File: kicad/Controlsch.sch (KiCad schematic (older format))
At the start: 8 parts

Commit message: Updates and new features
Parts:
- added C303: 10μF, symbol Device:C
- added D301: LED_RAGB, symbol Device:LED_RAGB
- added Q301, Q302, Q303: Q_NMOS_DGS, symbol Device:Q_NMOS_DGS
- added R302: 10kΩ, Resistor_SMD:R_0805_2012Metric, symbol Device:R
- added R303: 1kΩ, Resistor_SMD:R_0805_2012Metric, symbol Device:R
- added R304, R305, R306: 470Ω, Resistor_SMD:R_0805_2012Metric, symbol Device:R
- added SW301: SW_SPST, symbol Switch:SW_SPST
- added U303: 7414, symbol 74xx_IEEE:7414
- C301, C302: renamed from C?; footprint (none) -> Capacitor_SMD:C_0805_2012Metric
- R301: renamed from R?; footprint (none) -> Resistor_SMD:R_0805_2012Metric
- gave numbers to parts that had none: 5
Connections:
- net labels added: LED_BLU, LED_GRN, LED_RED, RxD_DIN, SW_01, TxD_DOUT
- wire segments 31 -> 82
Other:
- note added: "Board Temperature\n- There is an internal temperature \n sensor in the MCU"

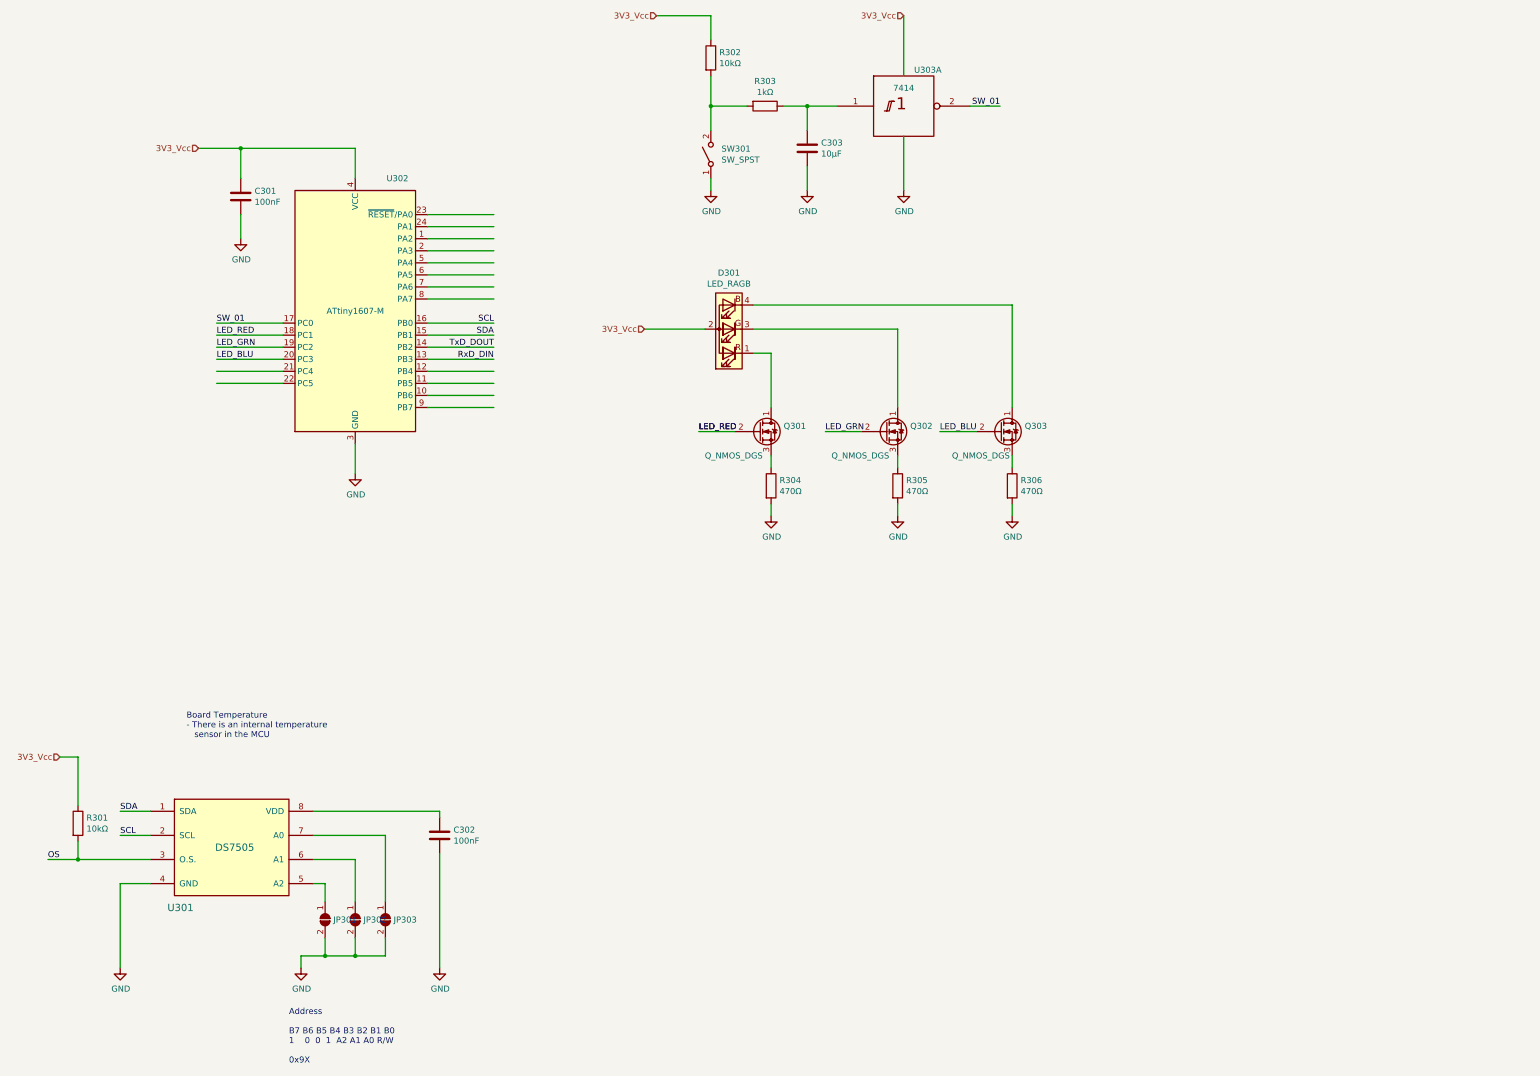
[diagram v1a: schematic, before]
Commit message: Updated the addresssing of the LCD
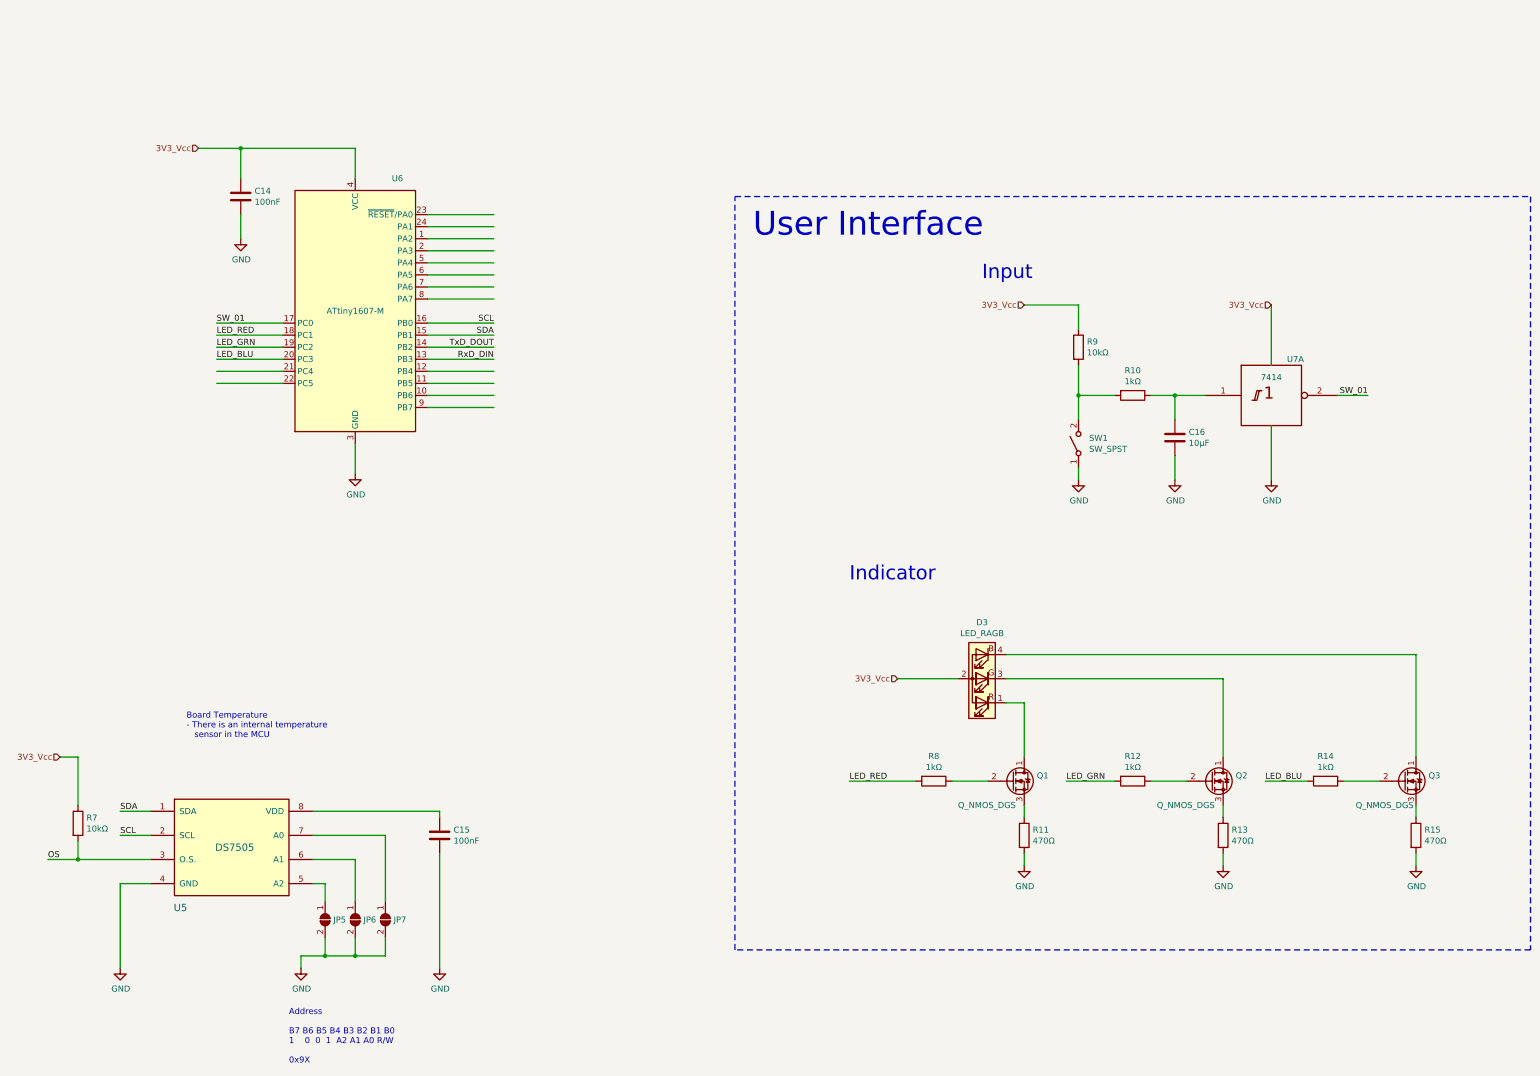
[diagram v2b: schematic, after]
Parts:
- added R12, R14, R8: 1kΩ, Resistor_SMD:R_0805_2012Metric, symbol Device:R
- renumbered C301 to C14, C302 to C15, C303 to C16, D301 to D3, JP301 to JP5, JP302 to JP6, JP303 to JP7, Q301 to Q1, Q302 to Q2, Q303 to Q3, R303 to R10, R304 to R11, R305 to R13, R306 to R15, R301 to R7, R302 to R9, SW301 to SW1, U301 to U5, U302 to U6, U303 to U7
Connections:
- wire segments 82 -> 85
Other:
- note added: "Indicator"
- note added: "Input"
- note added: "User Interface"
- moved on the sheet: C16, D3, Q1, Q2, Q3, R10, R11, R13, R15, R9, SW1, U7A

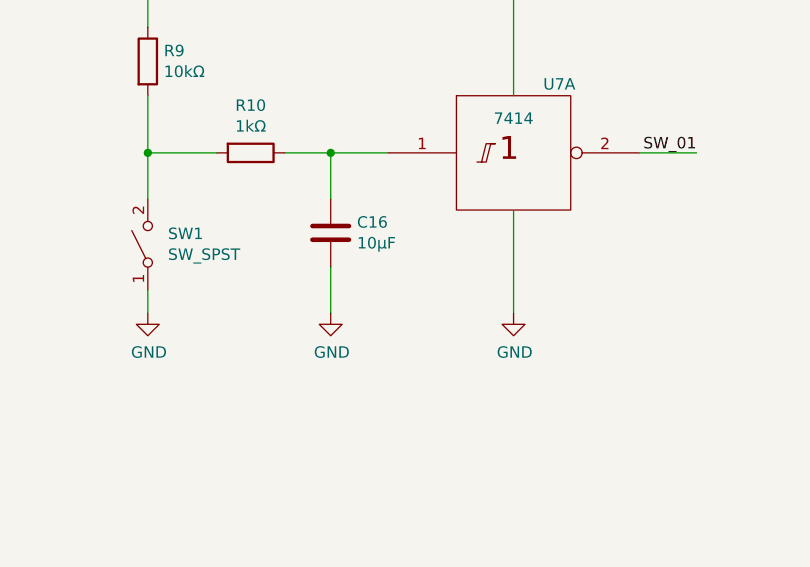
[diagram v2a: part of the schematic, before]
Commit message: Added a note about the capacitor for the de-bounce circuit
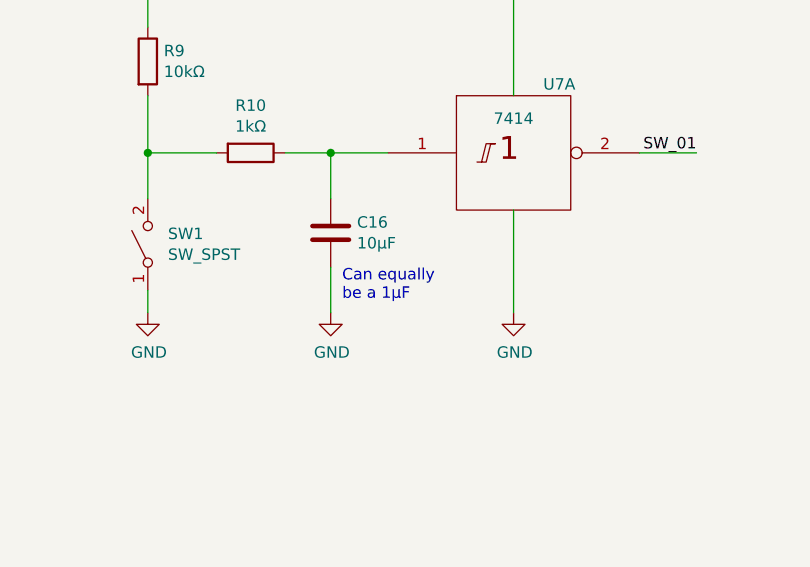
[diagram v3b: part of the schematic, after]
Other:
- note added: "Can equally \nbe a 1μF"
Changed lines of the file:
@@
 Text Notes 11200 3100 0    118  ~ 0
 Input
+Text Notes 12850 4700 0    50   ~ 0
+Can equally \nbe a 1μF
 $EndSCHEMATC

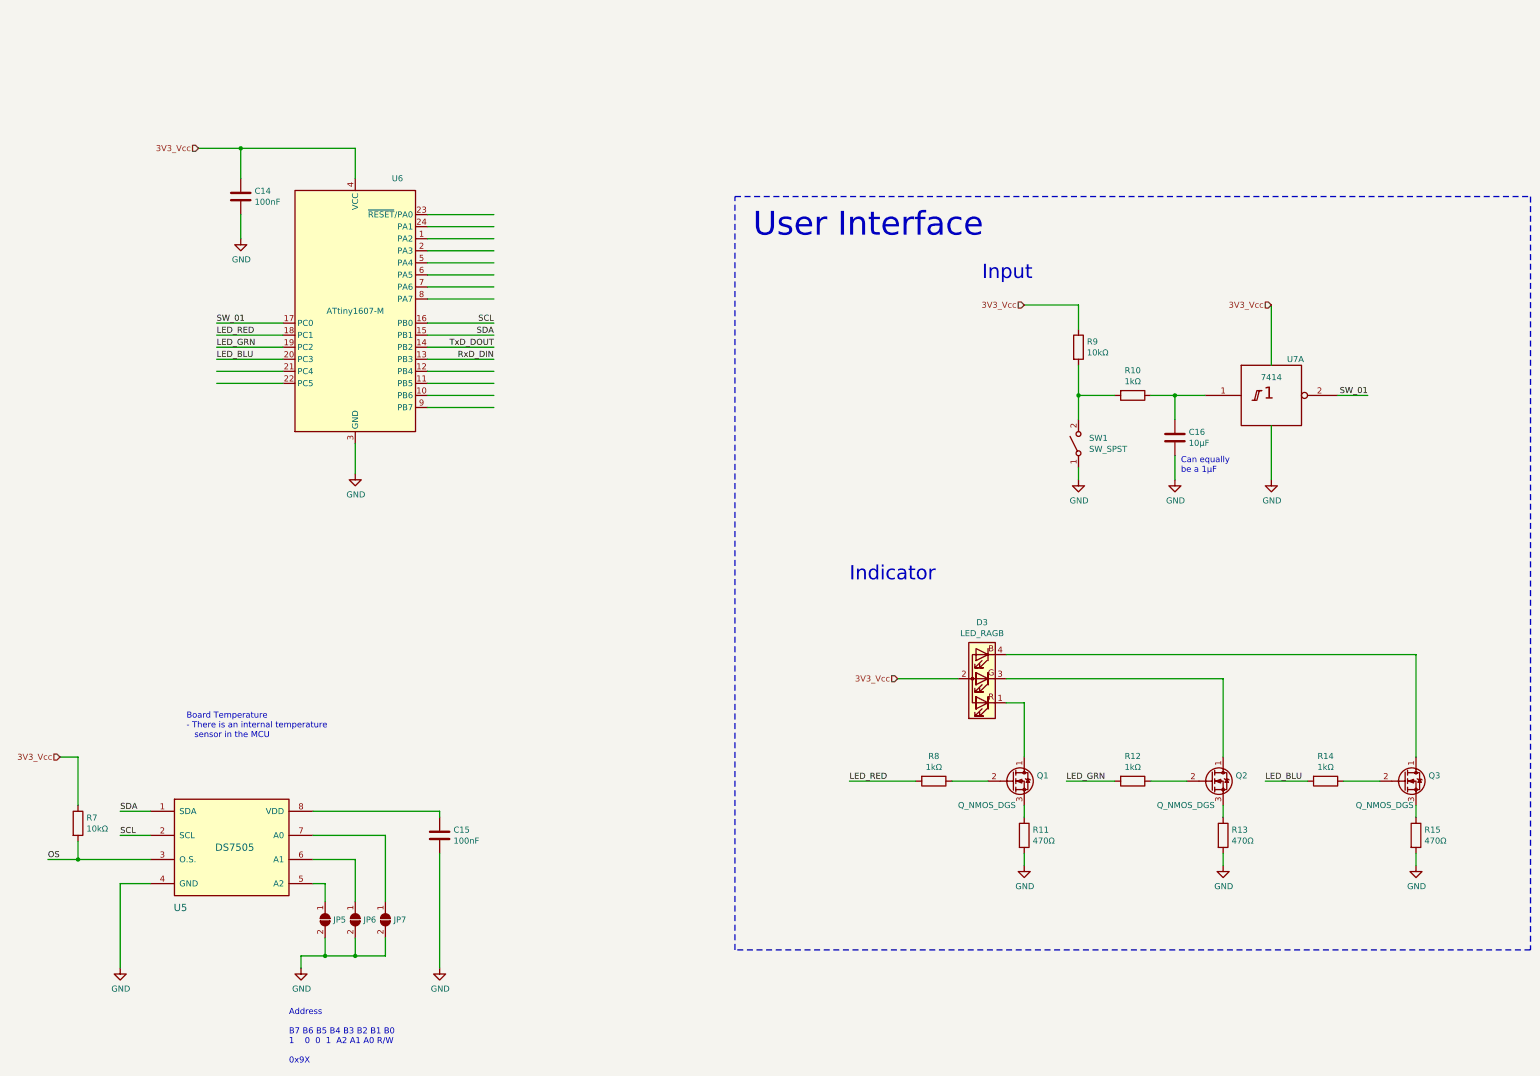
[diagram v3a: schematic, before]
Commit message: Updates the RC selection for the switch debounce
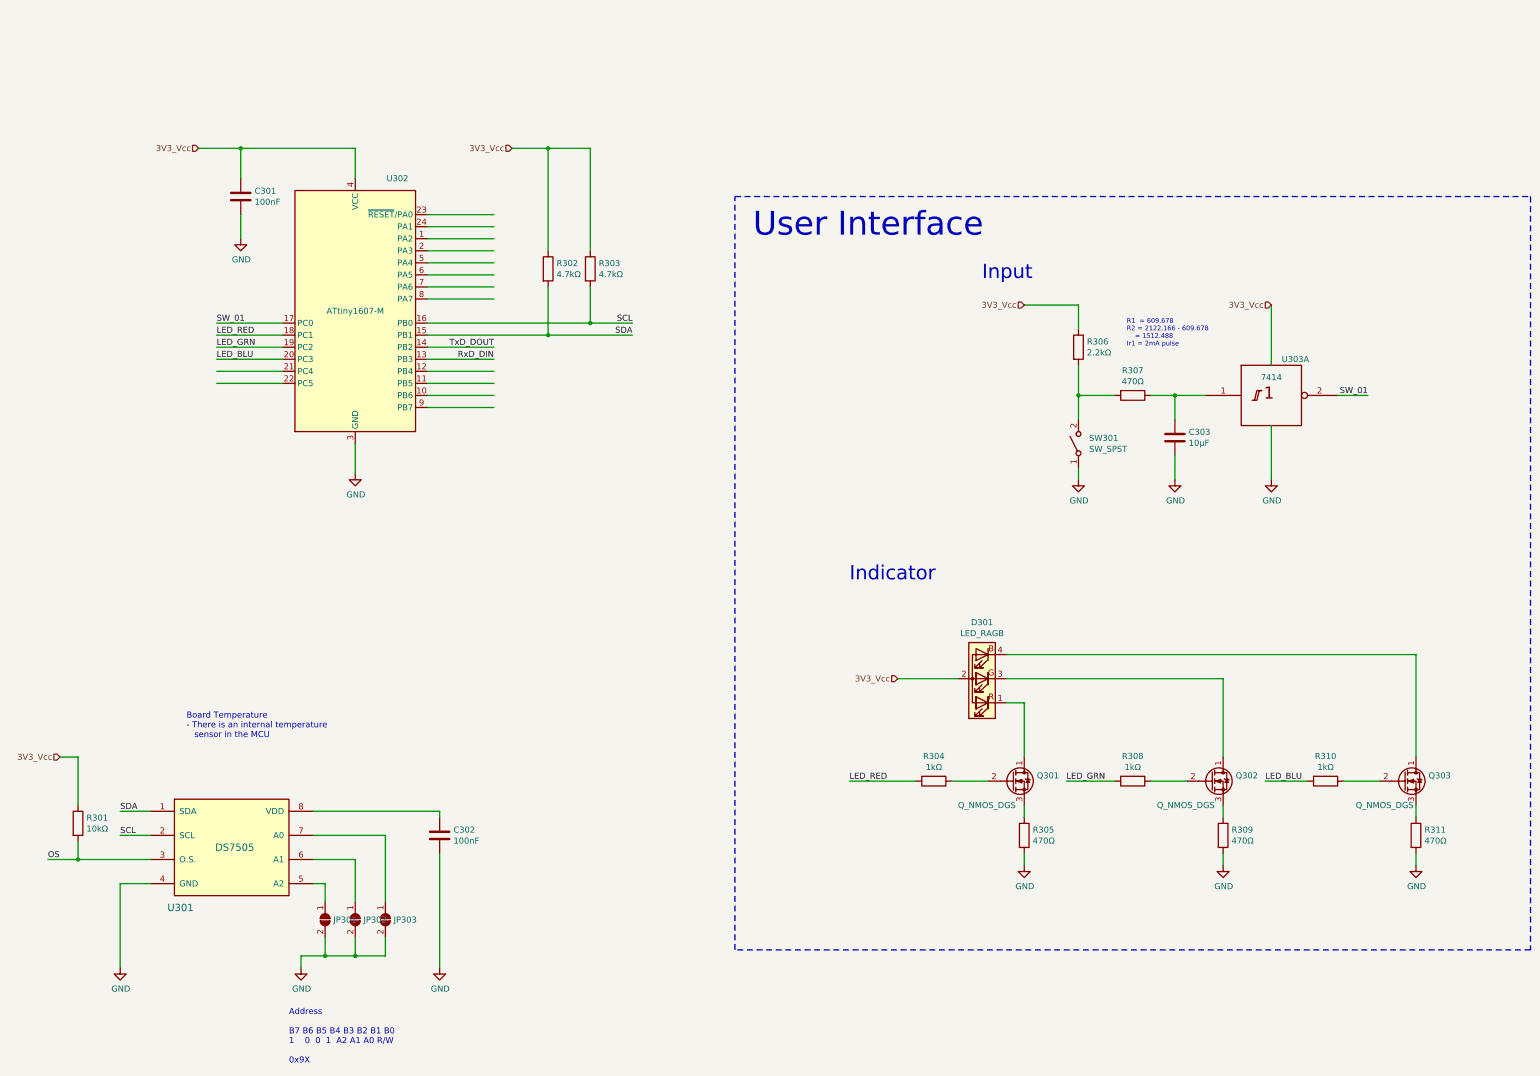
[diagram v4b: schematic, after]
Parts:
- added R302, R303: 4.7kΩ, Resistor_SMD:R_0805_2012Metric, symbol Device:R
- C303: renamed from C16; footprint (none) -> Capacitor_SMD:C_0805_2012Metric
- R306: renamed from R9; value 10kΩ -> 2.2kΩ
- R307: renamed from R10; value 1kΩ -> 470Ω
- renumbered C14 to C301, C15 to C302, D3 to D301, JP5 to JP301, JP6 to JP302, JP7 to JP303, Q1 to Q301, Q2 to Q302, Q3 to Q303, R7 to R301, R8 to R304, R11 to R305, R12 to R308, R13 to R309, R14 to R310, R15 to R311, SW1 to SW301, U5 to U301, U6 to U302, U7 to U303
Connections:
- wire segments 85 -> 93
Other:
- note added: "R1 = 609.678\nR2 = 2122.166 - 609.678\n = 1512.488\nIr1 = 2mA pulse\n"
- note removed: "Can equally \nbe a 1μF"
